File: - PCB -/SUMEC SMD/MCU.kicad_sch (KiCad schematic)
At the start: 15 parts, among them J2 USB3090-XX-X_REVE, SW2 SW_Push, SW4 SW_Push, U9 ESP32-S3-WROOM-1

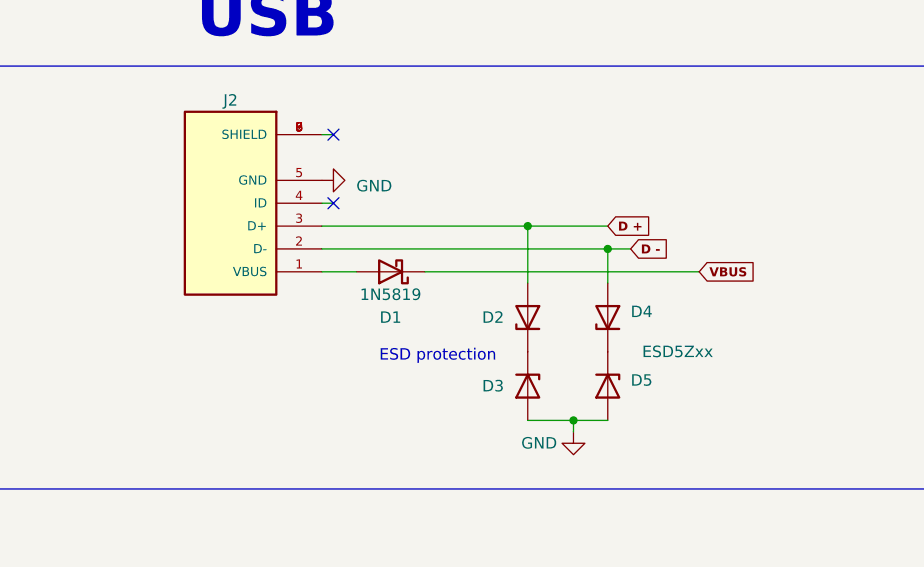
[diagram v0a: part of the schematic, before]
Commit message: pcb schematic update LIDAR sensors
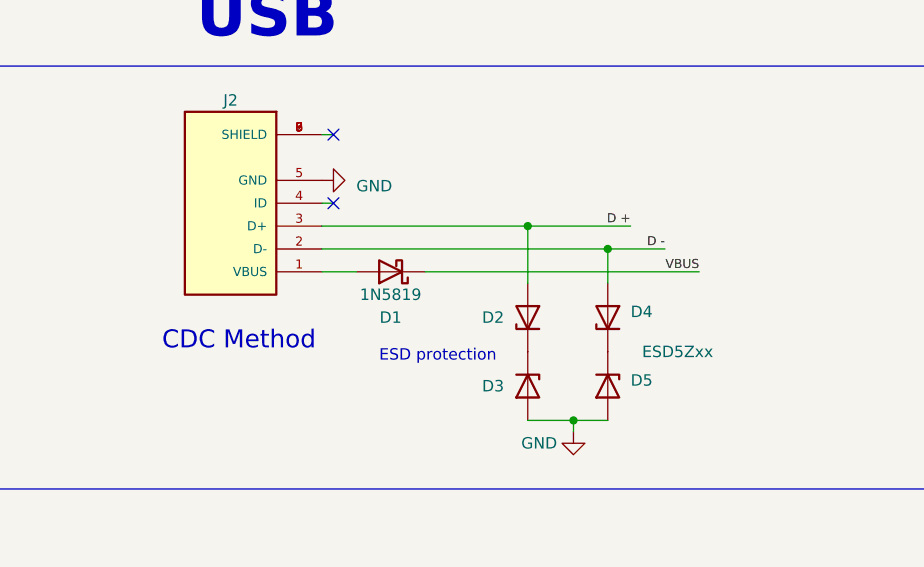
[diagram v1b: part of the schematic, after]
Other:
- note added: "CDC Method"
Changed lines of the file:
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@@
     (stroke (width 0) (type default))
   )
-  (wire (pts (xy 466.09 168.91) (xy 474.98 168.91))
+  (wire (pts (xy 466.09 168.91) (xy 477.52 168.91))
     (stroke (width 0) (type default))
   )
@@
     (stroke (width 0) (type default))
   )
-  (wire (pts (xy 474.98 171.45) (xy 477.52 171.45))
+  (wire (pts (xy 474.98 171.45) (xy 481.33 171.45))
     (stroke (width 0) (type default))
   )
@@
     (effects (font (size 1.5 1.5) italic) (justify left bottom))
   )
+  (text "CDC Method" (at 425.45 182.88 0)
+    (effects (font (size 2 2)) (justify left bottom))
+  )
   (text "MICRO-B USB Connector" (at 355.6 156.21 0)
     (effects (font (size 2 2)) (justify left bottom))
@@
     (effects (font (size 1.27 1.27) bold) (justify left bottom))
   )
+  (label "D -" (at 481.33 171.45 180) (fields_autoplaced)
+    (effects (font (size 1 1)) (justify right bottom))
+  )
   (label "BI2" (at 302.26 241.3 180) (fields_autoplaced)
     (effects (font (size 1 1)) (justify right bottom))
@@
     (effects (font (size 1 1)) (justify right bottom))
   )
+  (label "VBUS" (at 485.14 173.99 180) (fields_autoplaced)
+    (effects (font (size 1 1)) (justify right bottom))
+  )
   (label "QRE1113 C" (at 294.64 218.44 180) (fields_autoplaced)
     (effects (font (size 1 1)) (justify right bottom))
@@
     (effects (font (size 1 1)) (justify right bottom))
   )
+  (label "D +" (at 477.52 168.91 180) (fields_autoplaced)
+    (effects (font (size 1 1)) (justify right bottom))
+  )
   (label "TEST PROGRAM" (at 300.99 223.52 180) (fields_autoplaced)
     (effects (font (size 1 1)) (justify right bottom))
@@
       (effects (font (size 1.27 1.27)) (justify left) hide)
     )
-  )
-  (global_label "D -" (shape input) (at 477.52 171.45 0) (fields_autoplaced)
-    (effects (font (size 1 1) bold) (justify left))
-    (property "Intersheetrefs" "${INTERSHEET_REFS}" (at 483.1453 171.45 0)
-      (effects (font (size 1.27 1.27)) (justify left) hide)
-    )
-  )
-  (global_label "D +" (shape input) (at 474.98 168.91 0) (fields_autoplaced)
-    (effects (font (size 1 1) bold) (justify left))
-    (property "Intersheetrefs" "${INTERSHEET_REFS}" (at 480.6053 168.91 0)
-      (effects (font (size 1.27 1.27)) (justify left) hide)
-    )
-  )
-  (global_label "VBUS" (shape input) (at 485.14 173.99 0) (fields_autoplaced)
-    (effects (font (size 1 1) bold) (justify left))
-    (property "Intersheetrefs" "${INTERSHEET_REFS}" (at 491.6224 173.99 0)
-      (effects (font (size 1.27 1.27)) (justify left) hide)
-    )

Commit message: pcb schematic file cleanup
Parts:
- J2: footprint sumec-smd_library:MOLEX_47346-0001 -> GCT_USB3090-XX-X_REVE
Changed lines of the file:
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@@
+    )
+  )
+  (symbol (lib_id "sumec_library:USB3090-XX-X_REVE") (at 433.07 166.37 180) (unit 1)
+    (in_bom yes) (on_board yes) (dnp no) (fields_autoplaced)
+    (property "Reference" "J2" (at 433.07 152.4 0)
+      (effects (font (size 1.27 1.27)))
+    )
+    (property "Value" "USB3090-XX-X_REVE" (at 433.07 154.94 0)
+      (effects (font (size 1.27 1.27)))
+    )
+    (property "Footprint" "GCT_USB3090-XX-X_REVE" (at 433.07 166.37 0)
+      (effects (font (size 1.27 1.27)) (justify bottom) hide)
+    )
+    (property "Datasheet" "" (at 433.07 166.37 0)
+      (effects (font (size 1.27 1.27)) hide)
+    )
+    (property "MF" "Global Connector Technology" (at 433.07 166.37 0)
+      (effects (font (size 1.27 1.27)) (justify bottom) hide)
+    )
+    (property "Description" "\nUSB - micro AB USB 2.0 Receptacle Connector 5 Position Surface Mount, Right Angle; Through Hole, 2.35mm profile, 5 Pins, Horizontal, Bottom mount\n" (at 433.07 166.37 0)
+      (effects (font (size 1.27 1.27)) (justify bottom) hide)
+    )
+    (property "Package" "None" (at 433.07 166.37 0)
+      (effects (font (size 1.27 1.27)) (justify bottom) hide)
+    )
+    (property "Price" "None" (at 433.07 166.37 0)
+      (effects (font (size 1.27 1.27)) (justify bottom) hide)
+    )
+    (property "Check_prices" "https://www.snapeda.com/parts/USB3090-30-A/Global+Connector+Technology/view-part/?ref=eda" (at 433.07 166.37 0)
+      (effects (font (size 1.27 1.27)) (justify bottom) hide)
+    )
+    (property "SnapEDA_Link" "https://www.snapeda.com/parts/USB3090-30-A/Global+Connector+Technology/view-part/?ref=snap" (at 433.07 166.37 0)
+      (effects (font (size 1.27 1.27)) (justify bottom) hide)
+    )
+    (property "MP" "USB3090-30-A" (at 433.07 166.37 0)
+      (effects (font (size 1.27 1.27)) (justify bottom) hide)
+    )
+    (property "Availability" "In Stock" (at 433.07 166.37 0)
+      (effects (font (size 1.27 1.27)) (justify bottom) hide)
+    )
+    (property "MANUFACTURER" "GCT" (at 433.07 166.37 0)
+      (effects (font (size 1.27 1.27)) (justify bottom) hide)
+    )
+    (pin "1")
+    (pin "2")
+    (pin "3")
+    (pin "4")
+    (pin "5")
+    (pin "6")
+    (pin "7")
+    (pin "8")
+    (pin "9")
+    (instances
+      (project "sumec"
+        (path "/fc70a1a8-ed7c-4a0f-9b1a-f23293528385/11aa20d4-c4ff-49be-9179-c2911da50f67"
+          (reference "J2") (unit 1)
+        )
+      )
     )
   )
@@
         )
       )
-    )
-  )
-  (symbol (lib_id "sumec_library:USB3090-XX-X_REVE") (at 433.07 166.37 180) (unit 1)
-    (in_bom yes) (on_board yes) (dnp no)
-    (property "Reference" "J2" (at 433.07 154.94 0)
-      (effects (font (size 1.27 1.27)))
-    )
-    (property "Value" "USB3090-XX-X_REVE" (at 433.07 177.8 0)
-      (effects (font (size 1.27 1.27)) hide)
-    )
-    (property "Footprint" "sumec-smd_library:MOLEX_47346-0001" (at 433.07 166.37 0)
-      (effects (font (size 1.27 1.27)) (justify bottom) hide)
-    )
-    (property "Datasheet" "" (at 433.07 166.37 0)
-      (effects (font (size 1.27 1.27)) hide)
-    )
-    (property "MF" "Global Connector Technology" (at 433.07 166.37 0)
-      (effects (font (size 1.27 1.27)) (justify bottom) hide)
-    )
-    (property "Description" "\nUSB - micro AB USB 2.0 Receptacle Connector 5 Position Surface Mount, Right Angle; Through Hole, 2.35mm profile, 5 Pins, Horizontal, Bottom mount\n" (at 433.07 166.37 0)
-      (effects (font (size 1.27 1.27)) (justify bottom) hide)
-    )
-    (property "Package" "None" (at 433.07 166.37 0)
-      (effects (font (size 1.27 1.27)) (justify bottom) hide)
-    )
-    (property "Price" "None" (at 433.07 166.37 0)
-      (effects (font (size 1.27 1.27)) (justify bottom) hide)
-    )
-    (property "Check_prices" "https://www.snapeda.com/parts/USB3090-30-A/Global+Connector+Technology/view-part/?ref=eda" (at 433.07 166.37 0)
-      (effects (font (size 1.27 1.27)) (justify bottom) hide)
-    )
-    (property "SnapEDA_Link" "https://www.snapeda.com/parts/USB3090-30-A/Global+Connector+Technology/view-part/?ref=snap" (at 433.07 166.37 0)
-      (effects (font (size 1.27 1.27)) (justify bottom) hide)
-    )
-    (property "MP" "USB3090-30-A" (at 433.07 166.37 0)
-      (effects (font (size 1.27 1.27)) (justify bottom) hide)
-    )
-    (property "Availability" "In Stock" (at 433.07 166.37 0)
-      (effects (font (size 1.27 1.27)) (justify bottom) hide)
-    )
-    (property "MANUFACTURER" "GCT" (at 433.07 166.37 0)
-      (effects (font (size 1.27 1.27)) (justify bottom) hide)
-    )
-    (pin "1")
-    (pin "2")
-    (pin "3")
-    (pin "4")
-    (pin "5")
-    (pin "6")
-    (pin "7")
-    (pin "8")
-    (pin "9")
-    (instances
-      (project "sumec"
-        (path "/fc70a1a8-ed7c-4a0f-9b1a-f23293528385/11aa20d4-c4ff-49be-9179-c2911da50f67"
-          (reference "J2") (unit 1)
-        )
-        (path "/fc70a1a8-ed7c-4a0f-9b1a-f23293528385/f1a33fea-e0cc-4aaf-be45-30cc41af4eee"
-          (reference "J2") (unit 1)
-        )
-      )

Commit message: addition of manuals
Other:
- note added: "TF-LUNA MANUAL"
- note added: "USB - ESP CONNECTION"
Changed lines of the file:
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@@
   )
   (text "MICRO-B USB Connector" (at 355.6 156.21 0)
-    (effects (font (size 2 2)) (justify left bottom))
+    (effects (font (size 2 2) (thickness 0.4) bold italic) (justify left bottom))
   )
   (text "USB - " (at 674.37 473.71 0)
@@
     (effects (font (size 1.5 1.5) italic) (justify left bottom))
   )
+  (text "USB - ESP CONNECTION" (at 355.6 163.83 0)
+    (effects (font (face "Arial Unicode MS") (size 2 2) (thickness 0.254) bold) (justify left bottom) (href "https://docs.espressif.com/projects/esp-idf/en/latest/esp32s3/get-started/establish-serial-connection.html"))
+  )
   (text "Referenční board" (at 509.27 454.66 0)
     (effects (font (size 5 5) (thickness 1) bold italic) (justify left bottom))
@@
     (at 54.61 246.38 0)
     (effects (font (size 1.27 1.27)) (justify left bottom))
+  )
+  (text "TF-LUNA MANUAL" (at 355.6 170.18 0)
+    (effects (font (face "Arial Unicode MS") (size 2 2) (thickness 0.254) bold) (justify left bottom) (href "https://www.waveshare.com/wiki/TF-Luna_LiDAR_Range_Sensor"))
   )
   (text "ESD protection" (at 449.58 184.15 0)
@@
           (reference "#PWR04") (unit 1)
         )
-        (path "/fc70a1a8-ed7c-4a0f-9b1a-f23293528385/f1a33fea-e0cc-4aaf-be45-30cc41af4eee"
-          (reference "#PWR051") (unit 1)
-        )
       )
     )
@@
       (project "sumec"
         (path "/fc70a1a8-ed7c-4a0f-9b1a-f23293528385/11aa20d4-c4ff-49be-9179-c2911da50f67"
-          (reference "#PWR037") (unit 1)
-        )
-        (path "/fc70a1a8-ed7c-4a0f-9b1a-f23293528385/f1a33fea-e0cc-4aaf-be45-30cc41af4eee"
           (reference "#PWR037") (unit 1)
         )
@@
       (project "sumec"
         (path "/fc70a1a8-ed7c-4a0f-9b1a-f23293528385/11aa20d4-c4ff-49be-9179-c2911da50f67"
-          (reference "D1") (unit 1)
-        )
-        (path "/fc70a1a8-ed7c-4a0f-9b1a-f23293528385/f1a33fea-e0cc-4aaf-be45-30cc41af4eee"
           (reference "D1") (unit 1)
         )
@@
           (reference "D5") (unit 1)
         )
-        (path "/fc70a1a8-ed7c-4a0f-9b1a-f23293528385/f1a33fea-e0cc-4aaf-be45-30cc41af4eee"
-          (reference "D5") (unit 1)
-        )
       )
     )
@@
           (reference "D2") (unit 1)
         )
-        (path "/fc70a1a8-ed7c-4a0f-9b1a-f23293528385/f1a33fea-e0cc-4aaf-be45-30cc41af4eee"
-          (reference "D2") (unit 1)
-        )
       )
     )
@@
           (reference "#PWR01") (unit 1)
         )
-        (path "/fc70a1a8-ed7c-4a0f-9b1a-f23293528385/f1a33fea-e0cc-4aaf-be45-30cc41af4eee"
-          (reference "#PWR027") (unit 1)
-        )
       )
     )
@@
           (reference "SW4") (unit 1)
         )
-        (path "/fc70a1a8-ed7c-4a0f-9b1a-f23293528385/f1a33fea-e0cc-4aaf-be45-30cc41af4eee"
-          (reference "SW8") (unit 1)
-        )
       )
     )
@@
         (path "/fc70a1a8-ed7c-4a0f-9b1a-f23293528385/11aa20d4-c4ff-49be-9179-c2911da50f67"
           (reference "#PWR039") (unit 1)
-        )
-        (path "/fc70a1a8-ed7c-4a0f-9b1a-f23293528385/f1a33fea-e0cc-4aaf-be45-30cc41af4eee"
-          (reference "#PWR044") (unit 1)
         )
       )
@@
           (reference "D4") (unit 1)
         )
-        (path "/fc70a1a8-ed7c-4a0f-9b1a-f23293528385/f1a33fea-e0cc-4aaf-be45-30cc41af4eee"
-          (reference "D4") (unit 1)
-        )
       )
     )
@@
           (reference "C4") (unit 1)
         )
-        (path "/fc70a1a8-ed7c-4a0f-9b1a-f23293528385/f1a33fea-e0cc-4aaf-be45-30cc41af4eee"
-          (reference "C12") (unit 1)
-        )
       )
     )
@@
           (reference "D3") (unit 1)
         )
-        (path "/fc70a1a8-ed7c-4a0f-9b1a-f23293528385/f1a33fea-e0cc-4aaf-be45-30cc41af4eee"
-          (reference "D3") (unit 1)
-        )
       )
     )
@@
         (path "/fc70a1a8-ed7c-4a0f-9b1a-f23293528385/11aa20d4-c4ff-49be-9179-c2911da50f67"
           (reference "SW2") (unit 1)
-        )
-        (path "/fc70a1a8-ed7c-4a0f-9b1a-f23293528385/f1a33fea-e0cc-4aaf-be45-30cc41af4eee"
-          (reference "SW7") (unit 1)
         )
       )
@@
           (reference "C3") (unit 1)
         )
-        (path "/fc70a1a8-ed7c-4a0f-9b1a-f23293528385/f1a33fea-e0cc-4aaf-be45-30cc41af4eee"
-          (reference "C11") (unit 1)
-        )
-      )
+      )

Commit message: pcb schematic update
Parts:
- J2: footprint GCT_USB3090-XX-X_REVE -> sumec-smd_library:GCT_USB3090-XX-X_REVE
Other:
- note added: "EN=reset, BOOT=bootloader mode"
- note added: "If the device does not support the auto download mode, you need to get into the download mode manually. To do so, press and hold the BOOT button and then press the RESET button once. After that release the BOOT button."
- note removed: "EN=reset, BOOT=bootloader mode Hold BOOT, then press EN briefly to enter the bootloader, then release BOOT. This way you can flash a new firmware on it. Usually, the USB-to-UART adapter on the board can control these pins, so you don't have to do it manually."
- note removed: "TF-LUNA MANUAL"
- moved on the sheet: C?, SW2, SW4

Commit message: PCB cooler schematic and start of board making
bettr cal sol
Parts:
- added C18: 10uF.hb, Capacitor_SMD:C_1206_3216Metric, symbol Device:C_Polarized
- added C19: 1uF.hb, Capacitor_SMD:C_1206_3216Metric, symbol Device:C_Polarized
- added C?: 10uF.hbc, Capacitor_SMD:C_1206_3216Metric, symbol Device:C
- added C?: 0,5uF.hbc, Capacitor_SMD:C_1206_3216Metric, symbol Device:C
- added C?: 0,1uF.hbc, Capacitor_SMD:C_1206_3216Metric, symbol Device:C
- added D7.hbc1: D_Zener, Diode_SMD:D_1206_3216Metric, symbol Device:D_Zener
- added Q3: PMOS, Package_TO_SOT_THT:TO-220-3_Vertical, symbol Simulation_SPICE:PMOS
- added R25: 100k.hbc, Resistor_SMD:R_1206_3216Metric, symbol Device:R
- added U10: TB6612FNG, Package_SO:SSOP-24_5.3x8.2mm_P0.65mm, symbol Driver_Motor:TB6612FNG
- C?: value 0,1uF -> 0,1uF.mcu
- C? (x2): value 10uF -> 10uF.mcu
- C?: value 0,1uF -> 0,1uF.boot
- C?: value 0,1uF -> 0,1uF.en
- R8: value 10k -> 10k.mcu
- SW2, SW4: footprint Button_Switch_SMD:SW_SPST_B3U-1000P -> Button_Switch_THT:SW_PUSH_6mm
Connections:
- net X-SHUT 1 is gone; now on net AI1: U9.18 (GPIO10/TOUCH10/ADC1_CH9/FSPICS0/FSPIIO4/SUBSPICS0)
- net X-SHUT 3 is gone; now on net STBY: U9.20 (GPIO12/TOUCH12/ADC2_CH1/FSPICLK/FSPIIO6/SUBSPICLK)
- net +3V3: now also C18.1, C19.1, U10.20 (VCC)
- net AI1: now also U10.21 (AIN1); no longer U9.23 (GPIO21)
- net AI2: now also U9.17 (GPIO9/TOUCH9/ADC1_CH8/FSPIHD/SUBSPIHD), U10.22 (AIN2); no longer U9.11 (GPIO18/U1RXD/ADC2_CH7/CLK_OUT3)
- net BI1: now also U9.21 (GPIO13/TOUCH13/ADC2_CH2/FSPIQ/FSPIIO7/SUBSPIQ), U10.17 (BIN1); no longer U9.10 (GPIO17/U1TXD/ADC2_CH6)
- net BI2: now also U10.16 (BIN2)
- net GND: now also C18.2, C19.2, C?.2, C?.2, C?.2, R25.2, U10.10 (PGND2), U10.18 (GND), U10.3 (PGND1), U10.4 (PGND1), U10.9 (PGND2)
- net PWMA: now also U9.35 (MTMS/GPIO42), U10.23 (PWMA); no longer U9.34 (MTDI/GPIO41/CLK_OUT1)
- net PWMB: now also U9.34 (MTDI/GPIO41/CLK_OUT1), U10.15 (PWMB); no longer U9.35 (MTMS/GPIO42)
- net QRE1113 A: now also U9.4 (GPIO4/TOUCH4/ADC1_CH3); no longer U9.38 (GPIO2/TOUCH2/ADC1_CH1)
- net QRE1113 B: now also U9.5 (GPIO5/TOUCH5/ADC1_CH4); no longer U9.4 (GPIO4/TOUCH4/ADC1_CH3)
- net QRE1113 C: now also U9.6 (GPIO6/TOUCH6/ADC1_CH5); no longer U9.5 (GPIO5/TOUCH5/ADC1_CH4)
- net QRE1113 D: now also U9.7 (GPIO7/TOUCH7/ADC1_CH6); no longer U9.6 (GPIO6/TOUCH6/ADC1_CH5)
- net SCL: now also U9.10 (GPIO17/U1TXD/ADC2_CH6); no longer U9.17 (GPIO9/TOUCH9/ADC1_CH8/FSPIHD/SUBSPIHD)
- net SDA: now also U9.11 (GPIO18/U1RXD/ADC2_CH7/CLK_OUT3); no longer U9.12 (GPIO8/TOUCH8/ADC1_CH7/SUBSPICS1)
- net STBY: now also U10.19 (STBY); no longer U9.21 (GPIO13/TOUCH13/ADC2_CH2/FSPIQ/FSPIIO7/SUBSPIQ)
- net TEST PROGRAM: now also U9.38 (GPIO2/TOUCH2/ADC1_CH1); no longer U9.7 (GPIO7/TOUCH7/ADC1_CH6)
- net RXD: no longer names the net of U9.36 (U0RXD/GPIO44/CLK_OUT2)
- net TXD: no longer names the net of U9.37 (U0TXD/GPIO43/CLK_OUT1)
- net VBUS renamed +5V
- net X-SHUT 2: no longer names the net of U9.19 (GPIO11/TOUCH11/ADC2_CH0/FSPID/FSPIIO5/SUBSPID)
- new net: D7.hbc1.2 (A), Q3.2 (G), R25.1
- new net +8V: Q3.1 (D)
- new net MOTOR 1 +: U10.1 (AO1), U10.2 (AO1)
- new net MOTOR 1 -: U10.5 (AO2), U10.6 (AO2)
- new net MOTOR 2 +: U10.11 (BO1), U10.12 (BO1)
- new net MOTOR 2 -: U10.7 (BO2), U10.8 (BO2)
- new net VM: C?.1, C?.1, C?.1, D7.hbc1.1 (K), Q3.3 (S), U10.13 (VM2), U10.14 (VM3), U10.24 (VM1)
- no-connect marks 9 -> 18
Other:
- note added: "Data transfer USB connector connected to ESP32 using CDC method"
- note added: "EXPLANATION"
- note added: "H-MŮSTEK"
- note added: "Motor Driver - TB6612FNG (IN1 and IN2) can be used to control the motor in one of four function modes: - CW, CCW, short-brake and stop. The two motor outputs (A and B) can be separately controlled, and the speed of each motor is controlled via a PWM input signal with a frequency up to 100kHz. The STBY pin should be pulled high to take the motor out of standby mode. Operating voltage: 2.7-5.5VDC m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"
- note added: "není toho hodně? mohli bysme to ulehčit."
- note removed: "DOWNLOADER -"
- note removed: "FT2232H – Hi-Speed Dual USB UART/FIFO IC"
- note removed: "REFERENCE"
- note removed: "Referenční board"
- note removed: "Smart RGB LED controller and emitter"
- note removed: "USB -"
- note removed: "VOLTAGE REGULATOR -"
- note removed: "https://docs.espressif.com/projects/esp-idf/en/latest/esp32s3/hw-reference/esp32s3/user-guide-devkitc-1.html"
- moved on the sheet: C?, D1, D2, D3, D4, D5, J2, R8, SW2, SW4, U9
